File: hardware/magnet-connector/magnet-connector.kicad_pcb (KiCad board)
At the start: 2 copper layers, 2.2 x 2.2 mm, 0 parts

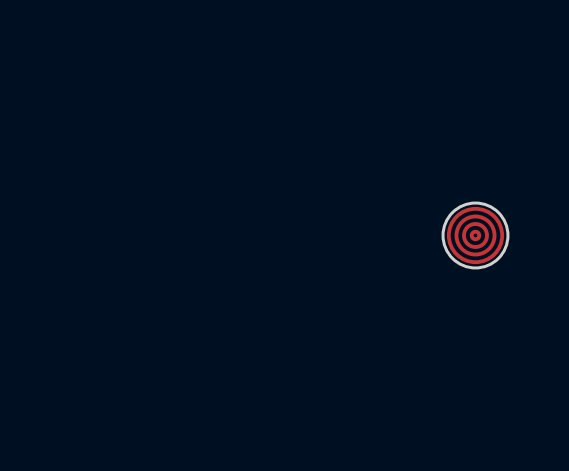
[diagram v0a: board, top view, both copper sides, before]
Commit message: Possible layout for magnet connector
Change-Id: I0a8c5969ca913f27f188b4b579de64d60ef6fdaa
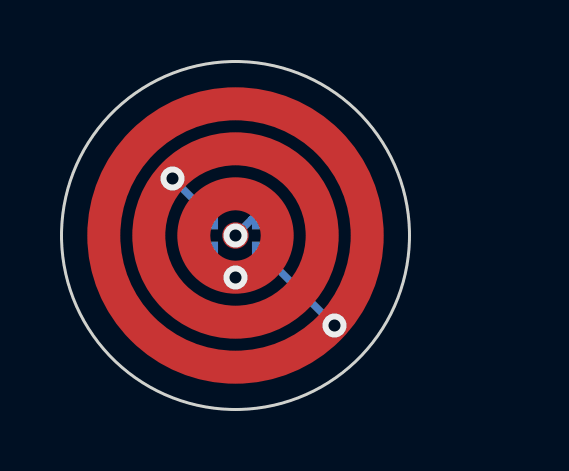
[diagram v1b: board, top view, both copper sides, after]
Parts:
- added U1: WS2812-2020, Homebrew:LED_WS2812-2020, B.Cu at (122.0, 100.0)
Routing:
- net GND: track 0.00 -> 3.44 mm, vias 0 -> 1
- net VCC: track 0.00 -> 1.83 mm, vias 0 -> 1
- net /IN: track 0.00 -> 1.28 mm, vias 0 -> 1
- net /OUT: track 0.00 -> 1.13 mm
- net (no net): vias 0 -> 1
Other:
- board size 2.2 x 2.2 mm -> 11.6 x 11.6 mm
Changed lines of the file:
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@@
   )
   (setup
+    (stackup
+      (layer "F.SilkS" (type "Top Silk Screen"))
+      (layer "F.Paste" (type "Top Solder Paste"))
+      (layer "F.Mask" (type "Top Solder Mask") (thickness 0.01))
+      (layer "F.Cu" (type "copper") (thickness 0.035))
+      (layer "dielectric 1" (type "core") (thickness 1.51) (material "FR4") (epsilon_r 4.5) (loss_tangent 0.02))
+      (layer "B.Cu" (type "copper") (thickness 0.035))
+      (layer "B.Mask" (type "Bottom Solder Mask") (thickness 0.01))
+      (layer "B.Paste" (type "Bottom Solder Paste"))
+      (layer "B.SilkS" (type "Bottom Silk Screen"))
+      (copper_finish "None")
+      (dielectric_constraints no)
+    )
     (pad_to_mask_clearance 0)
     (pcbplotparams
       (layerselection 0x00010fc_ffffffff)
       (disableapertmacros false)
-      (usegerberextensions false)
+      (usegerberextensions true)
       (usegerberattributes true)
       (usegerberadvancedattributes true)
-      (creategerberjobfile true)
+      (creategerberjobfile false)
       (svguseinch false)
       (svgprecision 6)
@@
       (psnegative false)
       (psa4output false)
-      (plotreference true)
-      (plotvalue true)
+      (plotreference false)
+      (plotvalue false)
       (plotinvisibletext false)
       (sketchpadsonfab false)
-      (subtractmaskfromsilk false)
+      (subtractmaskfromsilk true)
       (outputformat 1)
       (mirror false)
-      (drillshape 1)
+      (drillshape 0)
       (scaleselection 1)
-      (outputdirectory "")
+      (outputdirectory "gerber")
     )
   )
   (net 0 "")
-  (gr_circle (center 130 100) (end 130.635 100) (layer "F.Cu") (width 0.127) (fill none))
-  (gr_circle (center 130 100) (end 130.127 100) (layer "F.Cu") (width 0.127) (fill none))
-  (gr_circle (center 130 100) (end 130.889 100) (layer "F.Cu") (width 0.127) (fill none))
-  (gr_circle (center 130 100) (end 130.384 100) (layer "F.Cu") (width 0.127) (fill none))
-  (gr_circle (center 130 100) (end 130.635 100) (layer "F.Mask") (width 0.127) (fill none))
-  (gr_circle (center 130 100) (end 130.889 100) (layer "F.Mask") (width 0.127) (fill none))
-  (gr_circle (center 130 100) (end 130.127 100) (layer "F.Mask") (width 0.127) (fill none))
-  (gr_circle (center 130 100) (end 130.384 100) (layer "F.Mask") (width 0.127) (fill none))
-  (gr_circle (center 130 100) (end 130.9 100.6) (layer "Edge.Cuts") (width 0.1) (fill none))
+  (net 1 "/IN")
+  (net 2 "VCC")
+  (net 3 "/OUT")
+  (net 4 "GND")
+  (footprint "Homebrew:LED_WS2812-2020" (layer "B.Cu")
+    (at 121.983522 100 180)
+    (property "MANUFACTURER" "Worldsemi")
+    (property "Sheetfile" "magnet-connector.kicad_sch")
+    (property "Sheetname" "")
+    (attr through_hole)
+    (fp_text reference "U1" (at 1.17686 2.09129) (layer "B.SilkS")
+      (effects (font (size 1.00011 1.00011) (thickness 0.15)) (justify mirror))
+    )
+    (fp_text value "WS2812-2020" (at 7.355145 -1.842715) (layer "B.Fab")
+      (effects (font (size 1.000591 1.000591) (thickness 0.15)) (justify mirror))
+    )
+    (fp_line (start -0.3 -1) (end 0.3 -1) (layer "B.SilkS") (width 0.127))
+    (fp_line (start -0.3 1) (end 0.3 1) (layer "B.SilkS") (width 0.127))
+    (fp_circle (center -1.77 0.63) (end -1.667044 0.63) (layer "B.SilkS") (width 0.2) (fill none))
+    (fp_line (start -1.515 1.25) (end -1.515 -1.25) (layer "B.CrtYd") (width 0.05))
+    (fp_line (start 1.515 -1.25) (end 1.515 1.25) (layer "B.CrtYd") (width 0.05))
+    (fp_line (start -1.515 -1.25) (end 1.515 -1.25) (layer "B.CrtYd") (width 0.05))
+    (fp_line (start 1.515 1.25) (end -1.515 1.25) (layer "B.CrtYd") (width 0.05))
+    (fp_line (start -1.1 -1) (end -1.1 1) (layer "B.Fab") (width 0.127))
+    (fp_line (start -1.1 1) (end 1.1 1) (layer "B.Fab") (width 0.127))
+    (fp_line (start 1.1 1) (end 1.1 -1) (layer "B.Fab") (width 0.127))
+    (fp_line (start 1.1 -1) (end -1.1 -1) (layer "B.Fab") (width 0.127))
+    (fp_circle (center -1.77 0.63) (end -1.667044 0.63) (layer "B.Fab") (width 0.2) (fill none))
+    (pad "1" smd rect locked (at -0.915 0.55 180) (size 0.7 0.7) (layers "B.Cu" "B.Paste" "B.Mask")
+      (pinfunction "DO") (pintype "output"))
+    (pad "2" smd rect locked (at -0.915 -0.55 180) (size 0.7 0.7) (layers "B.Cu" "B.Paste" "B.Mask")
+      (net 4 "GND") (pinfunction "GND") (pintype "power_in"))
+    (pad "3" smd rect locked (at 0.915 -0.55) (size 0.7 0.7) (layers "B.Cu" "B.Paste" "B.Mask")
+      (net 1 "/IN") (pinfunction "DI") (pintype "input"))
+    (pad "4" smd rect locked (at 0.915 0.55) (size 0.7 0.7) (layers "B.Cu" "B.Paste" "B.Mask")
+      (net 2 "VCC") (pinfunction "VDD") (pintype "power_in"))
+  )
+  (gr_circle (center 122 100) (end 124.89 100) (layer "F.Cu") (width 1.1) (fill none))
+  (gr_circle (center 122 100) (end 122.39 100) (layer "F.Cu") (width 0.1) (fill solid))
+  (gr_circle (center 122 100) (end 126.39 100) (layer "F.Cu") (width 1.1) (fill none))
+  (gr_circle (center 122 100) (end 123.39 100) (layer "F.Cu") (width 1.1) (fill none))
+  (gr_circle (center 122 100) (end 124.89 100) (layer "F.Mask") (width 1.1) (fill none))
+  (gr_circle (center 122 100) (end 126.39 100) (layer "F.Mask") (width 1.1) (fill none))
+  (gr_circle (center 122 100) (end 122.39 100) (layer "F.Mask") (width 0.1) (fill solid))
+  (gr_circle (center 122 100) (end 123.39 100) (layer "F.Mask") (width 1.1) (fill none))
+  (gr_line (start 122 100) (end 127 100) (layer "Dwgs.User") (width 0.05))
+  (gr_circle (center 122 100) (end 127.8 100) (layer "Edge.Cuts") (width 0.1) (fill none))
+  (via (at 122 100) (size 0.8) (drill 0.4) (layers "F.Cu" "B.Cu") (free) (net 0))
+  (via (at 122 101.4) (size 0.8) (drill 0.4) (layers "F.Cu" "B.Cu") (net 1))
+  (segment (start 121.068522 100.55) (end 121.15 100.55) (width 0.25) (layer "B.Cu") (net 1))
+  (segment (start 121.15 100.55) (end 122 101.4) (width 0.25) (layer "B.Cu") (net 1))
+  (via (at 119.9 98.1) (size 0.8) (drill 0.4) (layers "F.Cu" "B.Cu") (net 2))
+  (segment (start 121.068522 99.268522) (end 119.9 98.1) (width 0.25) (layer "B.Cu") (net 2))
+  (segment (start 121.068522 99.45) (end 121.068522 99.268522) (width 0.25) (layer "B.Cu") (net 2))
+  (segment (start 122.898522 99.45) (end 122.55 99.45) (width 0.25) (layer "B.Cu") (net 3))
+  (segment (start 122.55 99.45) (end 122 100) (width 0.25) (layer "B.Cu") (net 3))
+  (via (at 125.3 103) (size 0.8) (drill 0.4) (layers "F.Cu" "B.Cu") (net 4))
+  (segment (start 122.898522 100.55) (end 122.898522 100.598522) (width 0.25) (layer "B.Cu") (net 4))
+  (segment (start 122.898522 100.598522) (end 125.3 103) (width 0.25) (layer "B.Cu") (net 4))
 )

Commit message: Update magnet connector with correct dimensions
Change-Id: I8f117cb6aa70f2da7e4e38435df749311b8c2ee4
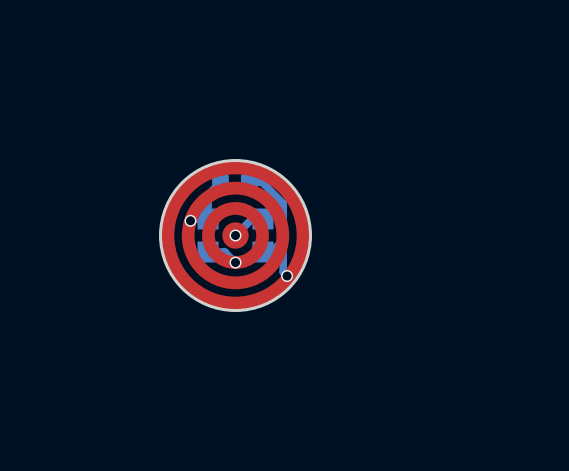
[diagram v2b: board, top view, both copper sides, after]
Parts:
- added C1: 100nF, Capacitor_SMD:C_0402_1005Metric, B.Cu at (122.0, 98.2)
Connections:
- U1 pad 1: (no net) -> /OUT
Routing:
- net GND: track 3.44 -> 4.74 mm
- net /OUT: track 1.13 -> 1.14 mm, vias 0 -> 1
- net (no net): vias 1 -> 0
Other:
- board size 11.6 x 11.6 mm -> 5 x 5 mm
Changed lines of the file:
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@@
   (net 4 "GND")
   (footprint "Homebrew:LED_WS2812-2020" (layer "B.Cu")
-    (at 121.983522 100 180)
+    (at 122 100 180)
     (property "MANUFACTURER" "Worldsemi")
+    (property "STANDARD" "Manufacturer Recommendations")
     (property "Sheetfile" "magnet-connector.kicad_sch")
     (property "Sheetname" "")
@@
     (fp_line (start -0.3 1) (end 0.3 1) (layer "B.SilkS") (width 0.127))
     (fp_circle (center -1.77 0.63) (end -1.667044 0.63) (layer "B.SilkS") (width 0.2) (fill none))
+    (fp_line (start -1.515 -1.25) (end 1.515 -1.25) (layer "B.CrtYd") (width 0.05))
+    (fp_line (start 1.515 1.25) (end -1.515 1.25) (layer "B.CrtYd") (width 0.05))
     (fp_line (start -1.515 1.25) (end -1.515 -1.25) (layer "B.CrtYd") (width 0.05))
     (fp_line (start 1.515 -1.25) (end 1.515 1.25) (layer "B.CrtYd") (width 0.05))
-    (fp_line (start -1.515 -1.25) (end 1.515 -1.25) (layer "B.CrtYd") (width 0.05))
-    (fp_line (start 1.515 1.25) (end -1.515 1.25) (layer "B.CrtYd") (width 0.05))
     (fp_line (start -1.1 -1) (end -1.1 1) (layer "B.Fab") (width 0.127))
     (fp_line (start -1.1 1) (end 1.1 1) (layer "B.Fab") (width 0.127))
+    (fp_line (start 1.1 -1) (end -1.1 -1) (layer "B.Fab") (width 0.127))
     (fp_line (start 1.1 1) (end 1.1 -1) (layer "B.Fab") (width 0.127))
-    (fp_line (start 1.1 -1) (end -1.1 -1) (layer "B.Fab") (width 0.127))
     (fp_circle (center -1.77 0.63) (end -1.667044 0.63) (layer "B.Fab") (width 0.2) (fill none))
-    (pad "1" smd rect locked (at -0.915 0.55 180) (size 0.7 0.7) (layers "B.Cu" "B.Paste" "B.Mask")
-      (pinfunction "DO") (pintype "output"))
-    (pad "2" smd rect locked (at -0.915 -0.55 180) (size 0.7 0.7) (layers "B.Cu" "B.Paste" "B.Mask")
+    (pad "1" smd rect (at -0.915 0.55 180) (size 0.7 0.7) (layers "B.Cu" "B.Paste" "B.Mask")
+      (net 3 "/OUT") (pinfunction "DO") (pintype "output"))
+    (pad "2" smd rect (at -0.915 -0.55 180) (size 0.7 0.7) (layers "B.Cu" "B.Paste" "B.Mask")
       (net 4 "GND") (pinfunction "GND") (pintype "power_in"))
-    (pad "3" smd rect locked (at 0.915 -0.55) (size 0.7 0.7) (layers "B.Cu" "B.Paste" "B.Mask")
+    (pad "3" smd rect (at 0.915 -0.55) (size 0.7 0.7) (layers "B.Cu" "B.Paste" "B.Mask")
       (net 1 "/IN") (pinfunction "DI") (pintype "input"))
-    (pad "4" smd rect locked (at 0.915 0.55) (size 0.7 0.7) (layers "B.Cu" "B.Paste" "B.Mask")
+    (pad "4" smd rect (at 0.915 0.55) (size 0.7 0.7) (layers "B.Cu" "B.Paste" "B.Mask")
       (net 2 "VCC") (pinfunction "VDD") (pintype "power_in"))
+    (model ":homebrew:WS2812-2020.STEP"
+      (offset (xyz 0 0 0.25))
+      (scale (xyz 1 1 1))
+      (rotate (xyz -90 0 0))
+    )
   )
-  (gr_circle (center 122 100) (end 124.89 100) (layer "F.Cu") (width 1.1) (fill none))
+  (footprint "Capacitor_SMD:C_0402_1005Metric" (layer "B.Cu")
+    (at 121.98 98.22)
+    (descr "Capacitor SMD 0402 (1005 Metric), square (rectangular) end terminal, IPC_7351 nominal, (Body size source: IPC-SM-782 page 76, https://www.pcb-3d.com/wordpress/wp-content/uploads/ipc-sm-782a_amendment_1_and_2.pdf), generated with kicad-footprint-generator")
+    (tags "capacitor")
+    (property "Sheetfile" "magnet-connector.kicad_sch")
+    (property "Sheetname" "")
+    (attr smd)
+    (fp_text reference "C1" (at 0 1.16) (layer "B.SilkS")
+      (effects (font (size 1 1) (thickness 0.15)) (justify mirror))
+    )
+    (fp_text value "100nF" (at 0 -1.16) (layer "B.Fab")
+      (effects (font (size 1 1) (thickness 0.15)) (justify mirror))
+    )
+    (fp_text user "${REFERENCE}" (at 0 0) (layer "B.Fab")
+      (effects (font (size 0.25 0.25) (thickness 0.04)) (justify mirror))
+    )
+    (fp_line (start -0.107836 0.36) (end 0.107836 0.36) (layer "B.SilkS") (width 0.12))
+    (fp_line (start -0.107836 -0.36) (end 0.107836 -0.36) (layer "B.SilkS") (width 0.12))
+    (fp_line (start 0.91 0.46) (end 0.91 -0.46) (layer "B.CrtYd") (width 0.05))
+    (fp_line (start -0.91 -0.46) (end -0.91 0.46) (layer "B.CrtYd") (width 0.05))
+    (fp_line (start 0.91 -0.46) (end -0.91 -0.46) (layer "B.CrtYd") (width 0.05))
+    (fp_line (start -0.91 0.46) (end 0.91 0.46) (layer "B.CrtYd") (width 0.05))
+    (fp_line (start -0.5 0.25) (end 0.5 0.25) (layer "B.Fab") (width 0.1))
+    (fp_line (start -0.5 -0.25) (end -0.5 0.25) (layer "B.Fab") (width 0.1))
+    (fp_line (start 0.5 -0.25) (end -0.5 -0.25) (layer "B.Fab") (width 0.1))
+    (fp_line (start 0.5 0.25) (end 0.5 -0.25) (layer "B.Fab") (width 0.1))
+    (pad "1" smd roundrect (at -0.48 0) (size 0.56 0.62) (layers "B.Cu" "B.Paste" "B.Mask") (roundrect_rratio 0.25)
+      (net 2 "VCC") (pintype "passive"))
+    (pad "2" smd roundrect (at 0.48 0) (size 0.56 0.62) (layers "B.Cu" "B.Paste" "B.Mask") (roundrect_rratio 0.25)
+      (net 4 "GND") (pintype "passive"))
+    (model "${KICAD6_3DMODEL_DIR}/Capacitor_SMD.3dshapes/C_0402_1005Metric.wrl"
+      (offset (xyz 0 0 0))
+      (scale (xyz 1 1 1))
+      (rotate (xyz 0 0 0))
+    )
+  )
+  (gr_circle (center 122 100) (end 123.5775 100) (layer "F.Cu") (width 0.425) (fill none))
   (gr_circle (center 122 100) (end 122.39 100) (layer "F.Cu") (width 0.1) (fill solid))
-  (gr_circle (center 122 100) (end 126.39 100) (layer "F.Cu") (width 1.1) (fill none))
-  (gr_circle (center 122 100) (end 123.39 100) (layer "F.Cu") (width 1.1) (fill none))
-  (gr_circle (center 122 100) (end 124.89 100) (layer "F.Mask") (width 1.1) (fill none))
-  (gr_circle (center 122 100) (end 126.39 100) (layer "F.Mask") (width 1.1) (fill none))
+  (gr_circle (center 122 100) (end 124.2525 100) (layer "F.Cu") (width 0.425) (fill none))
+  (gr_circle (center 122 100) (end 122.9025 100) (layer "F.Cu") (width 0.425) (fill none))
+  (gr_circle (center 122 100) (end 123.5775 100) (layer "F.Mask") (width 0.425) (fill none))
+  (gr_circle (center 122 100) (end 124.2525 100) (layer "F.Mask") (width 0.425) (fill none))
   (gr_circle (center 122 100) (end 122.39 100) (layer "F.Mask") (width 0.1) (fill solid))
-  (gr_circle (center 122 100) (end 123.39 100) (layer "F.Mask") (width 1.1) (fill none))
+  (gr_circle (center 122 100) (end 122.9025 100) (layer "F.Mask") (width 0.425) (fill none))
   (gr_line (start 122 100) (end 127 100) (layer "Dwgs.User") (width 0.05))
-  (gr_circle (center 122 100) (end 127.8 100) (layer "Edge.Cuts") (width 0.1) (fill none))
-  (via (at 122 100) (size 0.8) (drill 0.4) (layers "F.Cu" "B.Cu") (free) (net 0))
-  (via (at 122 101.4) (size 0.8) (drill 0.4) (layers "F.Cu" "B.Cu") (net 1))
-  (segment (start 121.068522 100.55) (end 121.15 100.55) (width 0.25) (layer "B.Cu") (net 1))
-  (segment (start 121.15 100.55) (end 122 101.4) (width 0.25) (layer "B.Cu") (net 1))
-  (via (at 119.9 98.1) (size 0.8) (drill 0.4) (layers "F.Cu" "B.Cu") (net 2))
-  (segment (start 121.068522 99.268522) (end 119.9 98.1) (width 0.25) (layer "B.Cu") (net 2))
-  (segment (start 121.068522 99.45) (end 121.068522 99.268522) (width 0.25) (layer "B.Cu") (net 2))
-  (segment (start 122.898522 99.45) (end 122.55 99.45) (width 0.25) (layer "B.Cu") (net 3))
-  (segment (start 122.55 99.45) (end 122 100) (width 0.25) (layer "B.Cu") (net 3))
-  (via (at 125.3 103) (size 0.8) (drill 0.4) (layers "F.Cu" "B.Cu") (net 4))
-  (segment (start 122.898522 100.55) (end 122.898522 100.598522) (width 0.25) (layer "B.Cu") (net 4))
-  (segment (start 122.898522 100.598522) (end 125.3 103) (width 0.25) (layer "B.Cu") (net 4))
+  (gr_circle (center 122 100) (end 124.5 100) (layer "Edge.Cuts") (width 0.1) (fill none))
+  (via (at 122 100.9025) (size 0.4) (drill 0.3) (layers "F.Cu" "B.Cu") (free) (net 1))
+  (segment (start 121.6475 100.55) (end 122 100.9025) (width 0.25) (layer "B.Cu") (net 1))
+  (segment (start 121.085 100.55) (end 121.6475 100.55) (width 0.25) (layer "B.Cu") (net 1))
+  (via (at 120.5 99.51) (size 0.4) (drill 0.3) (layers "F.Cu" "B.Cu") (free) (net 2))
+  (segment (start 121.085 98.635) (end 121.5 98.22) (width 0.25) (layer "B.Cu") (net 2))
+  (segment (start 121.085 99.45) (end 121.085 98.635) (width 0.25) (layer "B.Cu") (net 2))
+  (segment (start 121.085 99.45) (end 120.56 99.45) (width 0.25) (layer "B.Cu") (net 2))
+  (segment (start 120.56 99.45) (end 120.5 99.51) (width 0.25) (layer "B.Cu") (net 2))
+  (via (at 122 100) (size 0.4) (drill 0.3) (layers "F.Cu" "B.Cu") (free) (net 3))
+  (segment (start 122 100) (end 122.55 99.45) (width 0.25) (layer "B.Cu") (net 3))
+  (segment (start 122.55 99.45) (end 122.915 99.45) (width 0.25) (layer "B.Cu") (net 3))
+  (via (at 123.72 101.35) (size 0.4) (drill 0.3) (layers "F.Cu" "B.Cu") (free) (net 4))
+  (segment (start 123.589511 100.299511) (end 123.589511 101.219511) (width 0.25) (layer "B.Cu") (net 4))
+  (segment (start 123.589511 98.929511) (end 122.88 98.22) (width 0.25) (layer "B.Cu") (net 4))
+  (segment (start 123.589511 100.149511) (end 123.589511 98.929511) (width 0.25) (layer "B.Cu") (net 4))
+  (segment (start 122.88 98.22) (end 122.46 98.22) (width 0.25) (layer "B.Cu") (net 4))
+  (segment (start 123.589511 101.219511) (end 123.72 101.35) (width 0.25) (layer "B.Cu") (net 4))
+  (segment (start 122.915 100.55) (end 123.189022 100.55) (width 0.25) (layer "B.Cu") (net 4))
+  (segment (start 123.189022 100.55) (end 123.589511 100.149511) (width 0.25) (layer "B.Cu") (net 4))
+  (segment (start 123.589511 100.299511) (end 123.589511 100.149511) (width 0.25) (layer "B.Cu") (net 4))
 )
